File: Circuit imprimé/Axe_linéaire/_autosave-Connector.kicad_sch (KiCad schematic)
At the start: 5 parts, among them J1 Conn_01x14_Shielded, J2 Conn_01x14_Shielded

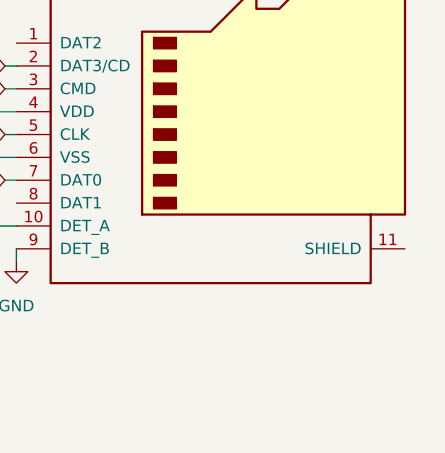
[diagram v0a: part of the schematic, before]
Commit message: Création du circuit imprimé
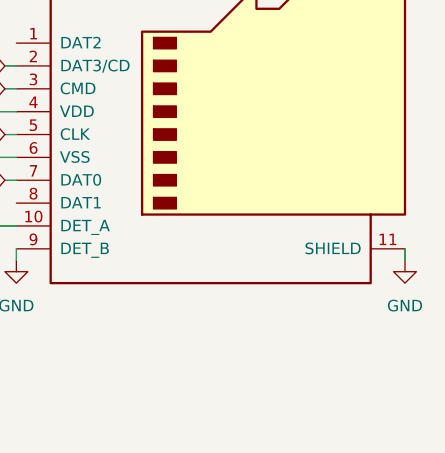
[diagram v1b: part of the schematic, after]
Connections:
- net GND: now also J?.11 (SHIELD)
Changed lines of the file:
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@@
+    (stroke (width 0) (type default) (color 0 0 0 0))
+  )
+  (wire (pts (xy 283.21 46.99) (xy 283.21 48.26))
     (stroke (width 0) (type default) (color 0 0 0 0))
   )
@@
       (effects (font (size 1.27 1.27)) hide)
     )
+    (pin "1")
+  )
+  (symbol (lib_id "power:GND") (at 283.21 48.26 0) (unit 1)
+    (in_bom yes) (on_board yes) (fields_autoplaced)
+    (property "Reference" "#PWR?" (id 0) (at 283.21 54.61 0)
+      (effects (font (size 1.27 1.27)) hide)
+    )
+    (property "Value" "GND" (id 1) (at 283.21 53.34 0))
+    (property "Footprint" "" (id 2) (at 283.21 48.26 0)
+      (effects (font (size 1.27 1.27)) hide)
+    )
+    (property "Datasheet" "" (id 3) (at 283.21 48.26 0)
+      (effects (font (size 1.27 1.27)) hide)
+    )
